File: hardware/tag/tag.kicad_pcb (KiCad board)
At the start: 2 copper layers, 50 x 52 mm, 119 parts, among them J1 USB_C_Receptacle_USB2.0_16P, J10 Conn_01x02, J2 BATTERY, J3 BLE_Conn, J4 SOURCE, J5 STM SWD, J6 I2C, J7 UART, J8 BLE SWD, J9 AUX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

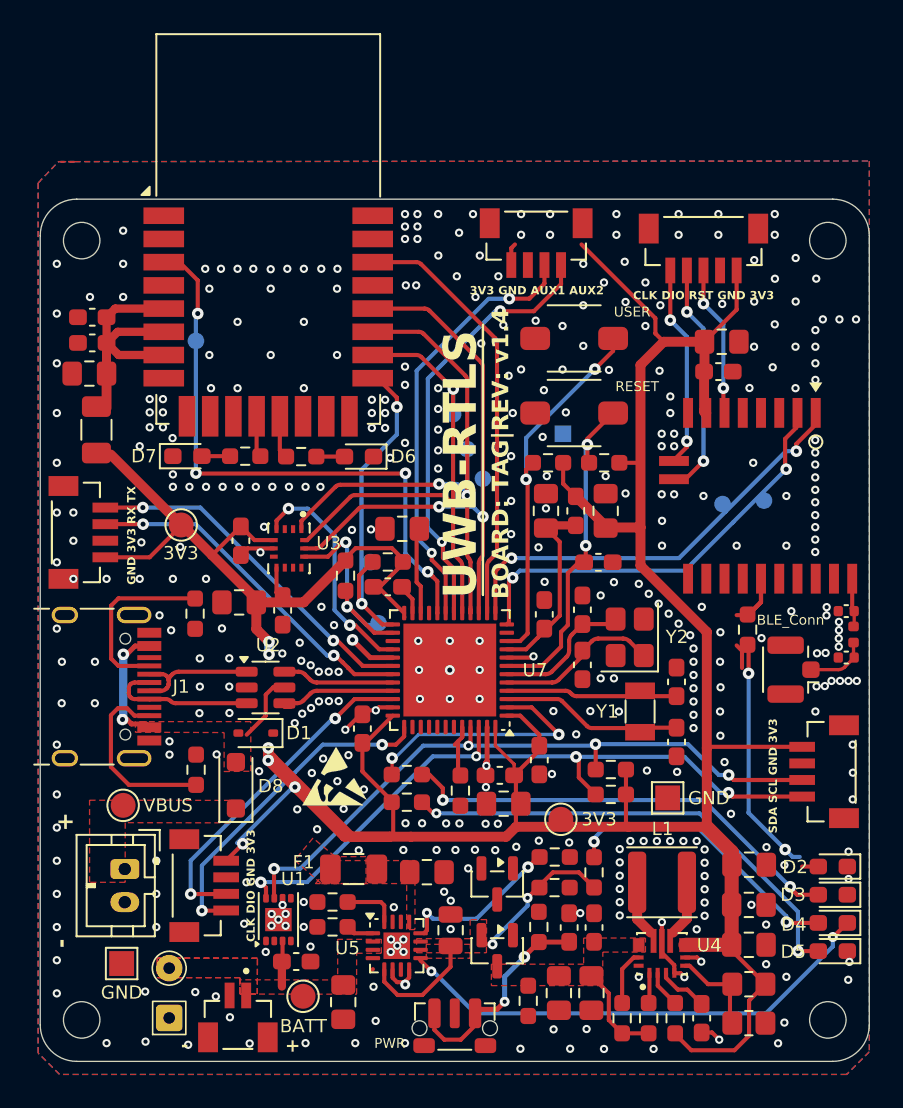
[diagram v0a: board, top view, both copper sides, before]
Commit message: update: add schottky diode to prevent the biased voltage back to soft latch circuit
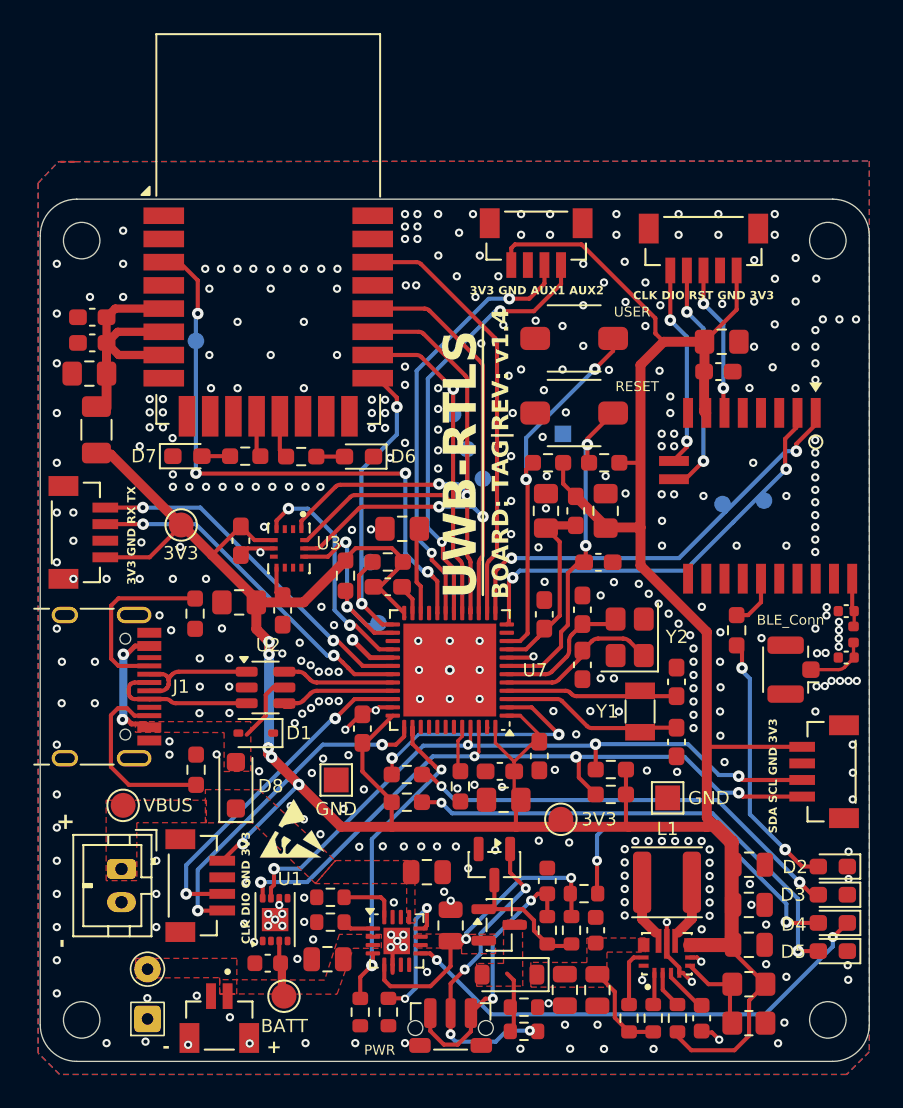
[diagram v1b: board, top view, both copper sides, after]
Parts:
- removed F1: Polyfuse_Small, Fuse:Fuse_1206_3216Metric
- added D9: D_Schottky, Diode_SMD:D_SOD-123, F.Cu at (59.3, 96.9)
- added R27: 10k, Resistor_SMD:R_0603_1608Metric, F.Cu at (50.3, 99.1)
- added R28: 10k, Resistor_SMD:R_0603_1608Metric, F.Cu at (60.2, 98.8)
- C1, C11, C12, C14, C2, C6, C8: footprint Capacitor_SMD:C_0805_2012Metric_Pad1.18x1.45mm_HandSolder -> Capacitor_SMD:C_0805_2012Metric
- C3, C4, C5, C7: footprint Capacitor_SMD:C_0603_1608Metric_Pad1.08x0.95mm_HandSolder -> Capacitor_SMD:C_0603_1608Metric
- J4: value SOURCE -> Conn_01x02
- R1, R11, R12, R13, R14, R19, R2, R5, R6, R8: footprint Resistor_SMD:R_0603_1608Metric_Pad0.98x0.95mm_HandSolder -> Resistor_SMD:R_0603_1608Metric
- moved TP5 17.0 mm to (48.9, 85.1)
- moved R5 13.7 mm to (52.0, 99.1), turned to -90 degrees
- moved C7 3.10 mm to (61.6, 91.2)
- moved R13 2.77 mm to (63.0, 94.2), turned to 90 degrees
- moved C8 2.75 mm to (48.3, 95.9), turned to 180 degrees
- moved R14 1.86 mm to (60.2, 100.3), turned to 180 degrees
- moved C4 1.72 mm to (44.7, 96.2), turned to 180 degrees
- moved Q3 1.56 mm to (58.7, 93.9), turned to 0 degrees
- moved R19 1.42 mm to (63.8, 92.0), turned to 180 degrees
- moved J10 1.31 mm to (37.5, 99.5)
- moved Q2 1.18 mm to (58.4, 90.2)
- moved TP7 1.15 mm to (45.7, 98.2)
- moved J2 1.12 mm to (41.8, 99.9)
- moved R16 0.66 mm to (73.0, 76.1)
- moved R12 0.55 mm to (61.6, 94.2), turned to -90 degrees
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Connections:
- Q3 pad 3: /LOAD -> Net-(D9-A)
- R14 pad 2: /LOAD -> Net-(D9-A)
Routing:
- net /CHARGE_EN: track 0.00 -> 20.5 mm, vias 0 -> 2
- net Net-(Q2-G): track 0.00 -> 19.5 mm, vias 0 -> 4
- net Net-(Q2-D): track 0.00 -> 8.39 mm
- net Net-(D9-A): track 0.00 -> 3.59 mm
- net Net-(C7-Pad2): track 13.3 -> 16.5 mm
- net GND: track 22.4 -> 19.5 mm, vias 394 -> 384
- net Net-(D4-A): track 17.8 -> 20.5 mm
- net unconnected-(U1-CELL-Pad2): track 2.49 -> 0.00 mm
- net Net-(U5-ILIM): track 9.67 -> 8.30 mm
- net /SYS: track 17.2 -> 18.5 mm
- net +3.3V: track 206.1 -> 205.1 mm
- net Net-(D3-A): track 28.3 -> 27.4 mm
- net Net-(D2-A): track 16.9 -> 16.1 mm
- net /PM_SCL: track 3.51 -> 2.87 mm
- net Net-(U7-BOOT0): track 3.34 -> 2.83 mm
- added copper zone on F.Cu, net Net-(D9-A)
- removed copper zone on F.Cu, net /VBUS_PROTECT
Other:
- board text added: "3V3 GND RX TX"
- board text added: "PRODUCTION BOARD REL: 2025-04-13"
- board text removed: "GND 3V3 RX TX"
- board text removed: "ID:"
- board text removed: "PRODUCTION BOARD REL: 2025-02-25"

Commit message: wip hardware changes
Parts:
- moved R19 5.67 mm to (58.7, 89.5)
- moved R13 5.40 mm to (58.7, 91.0), turned to 180 degrees
- moved Q2 5.23 mm to (62.1, 93.9)
- moved R12 3.28 mm to (62.1, 91.0), turned to 180 degrees
- moved C7 1.82 mm to (62.1, 89.5), turned to 180 degrees
- moved R5 0.24 mm to (51.8, 99.1)
- moved TP6 0.15 mm to (62.4, 87.3)
- moved C3 0.13 mm to (64.6, 94.3)
- turned Q3 to -90 degrees
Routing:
- net /SYS: track 18.5 -> 10.9 mm, vias 2 -> 0
- net Net-(C7-Pad2): track 16.5 -> 20.1 mm
- net Net-(D4-A): track 20.5 -> 22.3 mm
- net Net-(Q2-D): track 8.39 -> 7.12 mm
- net Net-(Q2-G): track 19.5 -> 20.0 mm
- net GND: vias 384 -> 387
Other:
- board text added: "PRODUCTION BOARD REL: 2025-05-06"
- board text removed: "PRODUCTION BOARD REL: 2025-04-13"

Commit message: feat: release final final hardware for tag + anchor
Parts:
- moved C6 0.29 mm to (54.0, 90.7)
- moved Q2 0.13 mm to (62.2, 93.7)
- moved Q3 0.13 mm to (58.7, 93.7)
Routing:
- net Net-(Q2-G): track 20.0 -> 18.6 mm
- net GND: vias 387 -> 393

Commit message: Update: schematic with new dimensions and additional notes
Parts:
- C7: value 100n -> 100n(TBD)
- D8, D9: value D_Schottky -> MBR230LSFT1G
- J4: value Conn_01x02 -> EXT VBUS
- R28: value 10k -> 1k(TBD)
- R8: value 10k -> NTC 10k
- moved R18 0.08 mm to (53.0, 84.8)
- moved R20 0.08 mm to (53.0, 86.5)
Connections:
- Q2 pad 1: Net-(Q2-G) -> /PWR_LATCH
- R14 pad 1: Net-(Q2-G) -> /PWR_LATCH
- SW1 pad 2: Net-(Q2-G) -> /PWR_LATCH
- U7 pad 39: unconnected-(U7-PB3-Pad39) -> /PWR_LATCH
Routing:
- net /PWR_LATCH: track 0.00 -> 35.8 mm, vias 0 -> 5
- net Net-(Q2-G): track 18.6 -> 0.00 mm, vias 4 -> 0
- net /CHARGE_EN: track 20.5 -> 19.6 mm
- net Net-(D3-A): track 27.4 -> 27.9 mm
